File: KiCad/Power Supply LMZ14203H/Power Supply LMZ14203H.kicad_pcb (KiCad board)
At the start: 2 copper layers, 61 x 47 mm, 39 parts, among them J1 Power IN, J2 Conn_02x03_Odd_Even, J3 Power OUT, U1 INA169, U2 LMZ14203H, U3 MCP3428, U4 INA169

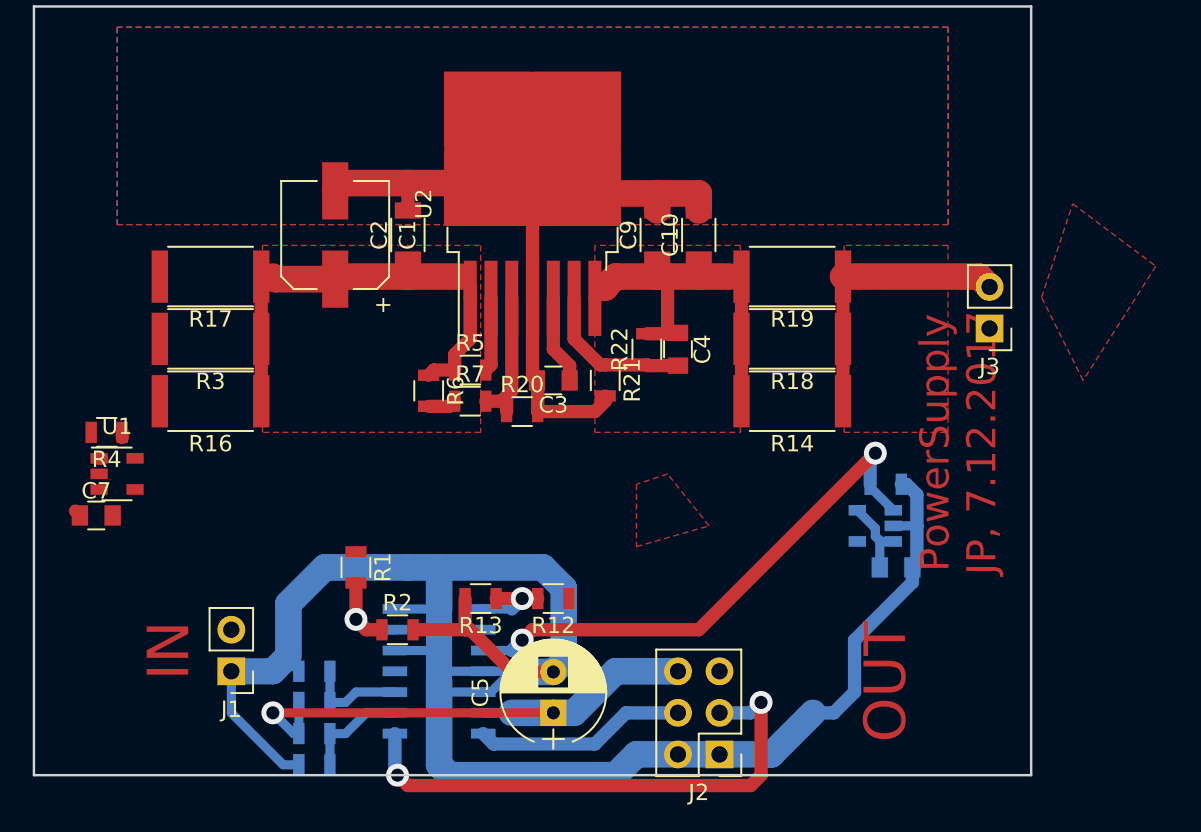
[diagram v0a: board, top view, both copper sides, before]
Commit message: LMZ14203H added
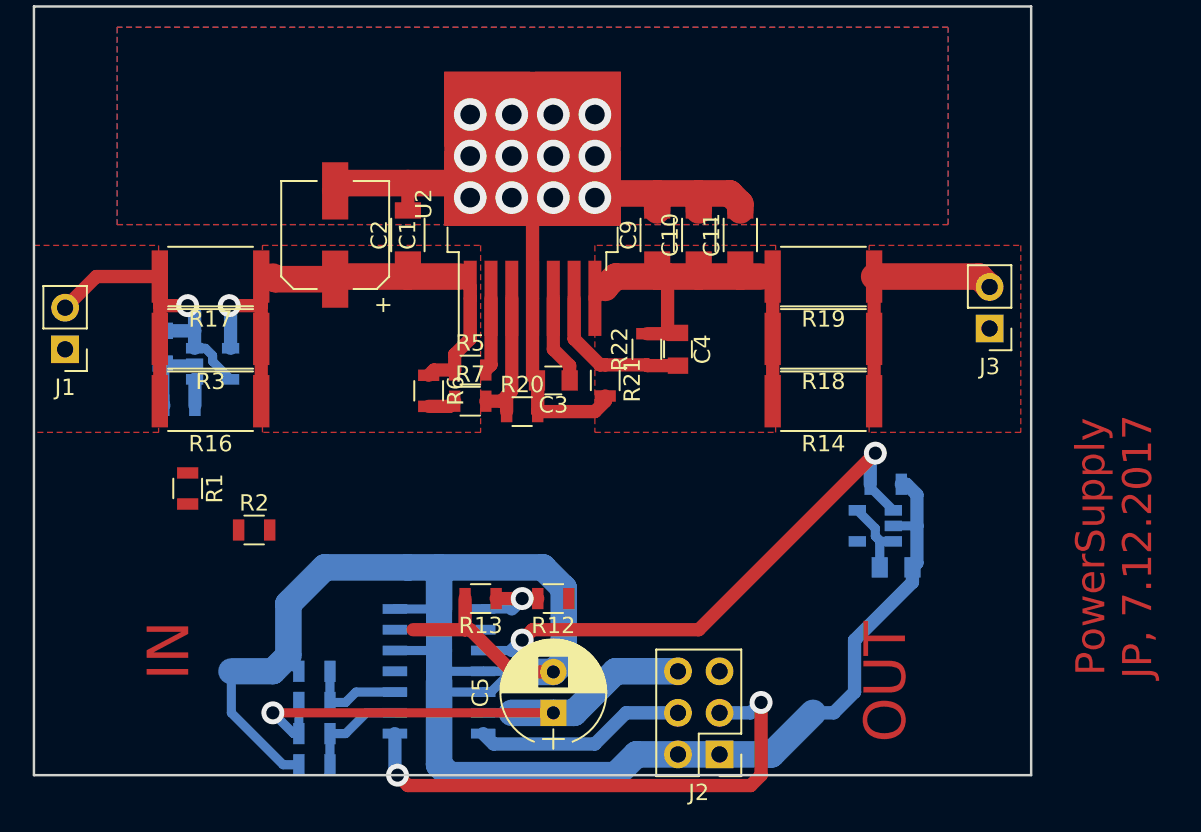
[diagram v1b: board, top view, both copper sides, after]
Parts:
- added C11: 47u/1-45mESR, Capacitors_SMD:C_1206, F.Cu at (161.3, 26.7)
- C7, R4, U1: moved to B.Cu
- moved J1 22.2 mm to (120.0, 33.7)
- moved R1 11.4 mm to (127.5, 42.2)
- moved C7 11.1 mm to (126.0, 33.5), turned to 90 degrees
- moved R2 10.7 mm to (131.6, 44.7)
- moved U1 8.91 mm to (129.0, 34.5)
- moved R4 4.74 mm to (127.0, 37.1)
- moved R14 1.91 mm to (166.4, 36.8)
- moved R18 1.91 mm to (166.4, 33.0)
- moved R19 1.91 mm to (166.4, 29.2)
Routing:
- net GNDA: track 181.8 -> 217.1 mm, vias 0 -> 12
- net Net-(C7-Pad2): track 0.00 -> 23.8 mm, vias 0 -> 1
- net IN_Voltage: track 6.72 -> 0.00 mm, vias 1 -> 0
- net Net-(C1-Pad1): track 29.0 -> 33.6 mm, vias 0 -> 1
- net Net-(C10-Pad1): track 31.2 -> 34.2 mm
- net Net-(J3-Pad2): track 16.8 -> 14.9 mm
- net IN_Current: track 0.46 -> 1.60 mm
- added copper zone on F.Cu, net Net-(C7-Pad2)
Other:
- net class Default: via_drill 0.8 -> 0.6

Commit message: Wirering
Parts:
- removed J2: Conn_02x03_Odd_Even, Pin_Headers:Pin_Header_Straight_2x03_Pitch2.54mm
- added C12: 10n, Capacitors_SMD:C_0805, F.Cu at (155.3, 90.1)
- added C13: 100n, Capacitors_SMD:C_0805, B.Cu at (121.9, 49.5)
- added C14: 100u, Capacitors_SMD:CP_Elec_6.3x7.7, F.Cu at (123.8, 44.3)
- added C16: 100n, Capacitors_SMD:C_0805, B.Cu at (121.9, 58.4)
- added C17: 47u, Capacitors_SMD:CP_Elec_6.3x5.8, F.Cu at (119.2, 54.0)
- added C18: 100n, Capacitors_SMD:C_0805, B.Cu at (144.8, 54.6)
- added C19: 10u, Capacitors_SMD:CP_Elec_4x5.8, F.Cu at (144.8, 57.8)
- added C20: 100n, Capacitors_SMD:C_0805, B.Cu at (134.6, 44.5)
- added C21: 10u, Capacitors_SMD:CP_Elec_4x5.8, F.Cu at (134.0, 43.8)
- added C22: 10u, Capacitors_SMD:CP_Elec_4x5.8, F.Cu at (173.4, 57.1)
- added C23: 10u, Capacitors_SMD:CP_Elec_4x5.8, F.Cu at (168.3, 52.1)
- added C24: 1u, Capacitors_SMD:C_0805, F.Cu at (149.0, 61.6)
- added D1: LED, Diodes_SMD:D_0805, F.Cu at (139.7, 85.7)
- added J4: OLED I2C, Pin_Headers:Pin_Header_Straight_1x04_Pitch2.54mm, F.Cu at (132.7, 52.7)
- added J5: PDI, Pin_Headers:Pin_Header_Straight_2x03_Pitch2.54mm, F.Cu at (179.1, 42.5)
- added J6: OLED, JPConnectors:FPC_30, F.Cu at (158.8, 57.1)
- added L1: 10u, Inductors_SMD:L_0805, F.Cu at (131.4, 49.5)
- added R23: 10k, Resistors_SMD:R_0805, F.Cu at (170.1, 80.3)
- added R24: 10k, Resistors_SMD:R_0805, F.Cu at (158.7, 90.2)
- added R25: 1M, Resistors_SMD:R_0805, F.Cu at (163.3, 89.9)
- added R26: 0, Resistors_SMD:R_0805, F.Cu at (149.2, 41.3)
- added SW1: SW_DIP_x01, Buttons_Switches_SMD:SW_SPST_B3SL-1002P, F.Cu at (184.2, 71.1)
- added U5: UA78M33, TO_SOT_Packages_SMD:TO-252-2_Rectifier, B.Cu at (120.0, 54.0)
- added U6: ATXMEGA32E5-AU, Housings_QFP:TQFP-32_7x7mm_Pitch0.8mm, B.Cu at (141.6, 48.3)
- C5: value 10u -> 100u; footprint Capacitors_THT:CP_Radial_D6.3mm_P2.50mm -> Capacitors_SMD:CP_Elec_6.3x7.7
- J1, J3: footprint Pin_Headers:Pin_Header_Straight_1x02_Pitch2.54mm -> Connectors_Terminal_Blocks:TerminalBlock_Altech_AK300-2_P5.00mm
- R10, R9: value 0 -> 2k2
- R11, R8: value 0 -> 10k
- U3: value MCP3428 -> L78M12; footprint Housings_SOIC:SOIC-14_3.9x8.7mm_Pitch1.27mm -> TO_SOT_Packages_SMD:TO-252-2_Rectifier
- moved C5 34.9 mm to (116.8, 44.5), turned to 270 degrees
- moved C6 30.1 mm to (121.3, 40.6), turned to 180 degrees
- moved U3 24.3 mm to (120.0, 45.1)
- moved R9 19.4 mm to (119.4, 64.5)
- moved R13 16.6 mm to (159.4, 40.0)
- moved R12 16.0 mm to (163.2, 40.0)
- moved R8 15.8 mm to (122.4, 64.5)
- moved C8 14.8 mm to (163.2, 34.3), turned to 90 degrees
- moved R10 13.1 mm to (122.9, 61.5)
- moved U4 10.0 mm to (166.4, 34.9), turned to 0 degrees
- moved J1 9.92 mm to (118.4, 23.9), turned to 270 degrees
- moved R11 9.83 mm to (126.5, 63.5)
- moved R2 7.70 mm to (138.1, 40.6)
- moved R15 7.24 mm to (164.5, 37.5), turned to 180 degrees
- moved R1 4.04 mm to (131.4, 41.3)
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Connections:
- C5 pad 1: +5V -> POWER_IN
- C5 pad 2: GNDA -> GND
- C6 pad 1: +5V -> POWER_IN
- C6 pad 2: GNDA -> GND
- C7 pad 2: Net-(C7-Pad2) -> POWER_IN
- J1 pad 2: Net-(C7-Pad2) -> POWER_IN
- J3 pad 1: GNDA -> POWER_OUT
- J3 pad 2: Net-(J3-Pad2) -> GNDA
- R1 pad 1: Net-(C7-Pad2) -> POWER_IN
- R10 pad 1: +5V -> SDA
- R10 pad 2: Net-(R10-Pad2) -> +3V3
- R11 pad 1: Net-(R10-Pad2) -> SWITCH
- R11 pad 2: GNDA -> Net-(R11-Pad2)
- R14 pad 1: Net-(J3-Pad2) -> POWER_OUT
- R16 pad 2: Net-(C7-Pad2) -> POWER_IN
- R17 pad 2: Net-(C7-Pad2) -> POWER_IN
- R18 pad 1: Net-(J3-Pad2) -> POWER_OUT
- R19 pad 1: Net-(J3-Pad2) -> POWER_OUT
- R3 pad 2: Net-(C7-Pad2) -> POWER_IN
- R8 pad 1: +5V -> LED
- R8 pad 2: Net-(R8-Pad2) -> Net-(D1-Pad1)
- R9 pad 1: Net-(R8-Pad2) -> SCK
- R9 pad 2: GNDA -> +3V3
- U1 pad 3: Net-(C7-Pad2) -> POWER_IN
- U1 pad 5: Net-(C7-Pad2) -> POWER_IN
- U3 pad 1: OUT_Voltage -> POWER_IN
- U3 pad 2: GNDA -> GND
- U3 pad 3: OUT_Current -> +12V
- U4 pad 4: Net-(J3-Pad2) -> POWER_OUT
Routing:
- net GNDA: track 217.1 -> 128.9 mm
- net GND: track 0.00 -> 54.0 mm, vias 0 -> 1
- net POWER_IN: track 0.00 -> 42.2 mm, vias 0 -> 1
- net /OLED_D4: track 0.00 -> 38.0 mm, vias 0 -> 1
- net /OLED_D2: track 0.00 -> 37.1 mm, vias 0 -> 1
- net /OLED_D0: track 0.00 -> 36.2 mm, vias 0 -> 3
- net +5V: track 36.1 -> 0.00 mm, vias 1 -> 0
- net /OLED_D6: track 0.00 -> 35.0 mm, vias 0 -> 1
- net SCL: track 32.6 -> 0.00 mm, vias 2 -> 0
- net OUT_Current: track 33.2 -> 1.65 mm, vias 2 -> 0
- net /OLED_D1: track 0.00 -> 31.4 mm, vias 0 -> 1
- net /OLED_D7: track 0.00 -> 30.5 mm, vias 0 -> 1
- net /OLED_D5: track 0.00 -> 26.1 mm, vias 0 -> 1
- net Net-(C7-Pad2): track 23.8 -> 0.00 mm, vias 1 -> 0
- net /OLED_D3: track 0.00 -> 22.9 mm, vias 0 -> 1
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- added copper zone on F.Cu, net POWER_IN
- added copper zone on F.Cu, net POWER_OUT
- removed copper zone on F.Cu, net Net-(C7-Pad2)
- removed copper zone on F.Cu, net Net-(J3-Pad2)
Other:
- board size 61 x 47 mm -> 71.8 x 51.4 mm
- board text removed: "IN"

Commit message: Wirering done
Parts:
- added REF**: MountingHole_3.2mm_M3, Mounting_Holes:MountingHole_3.2mm_M3, F.Cu at (122.6, 54.0)
- added REF**: MountingHole_3.2mm_M3, Mounting_Holes:MountingHole_3.2mm_M3, F.Cu at (59.7, 54.0)
- added REF**: MountingHole_3.2mm_M3, Mounting_Holes:MountingHole_3.2mm_M3, F.Cu at (61.0, 105.4)
- added REF**: MountingHole_3.2mm_M3, Mounting_Holes:MountingHole_3.2mm_M3, F.Cu at (122.6, 106.0)
- C24, L1, R1, R12, R13, R2, R24, R25: moved to B.Cu
- J4: footprint Pin_Headers:Pin_Header_Straight_1x04_Pitch2.54mm -> JPDisplays:OLED_0.96inch_128x64_I2C
- R11, R8: moved to F.Cu
- moved R12 87.1 mm to (88.3, 84.5), turned to 270 degrees
- moved R13 85.5 mm to (86.4, 84.5), turned to 90 degrees
- moved J5 78.9 mm to (118.1, 92.7), turned to 90 degrees
- moved J4 72.9 mm to (65.4, 80.6)
- moved C13 72.3 mm to (65.4, 94.6)
- moved C14 72.3 mm to (67.3, 89.4)
- moved C16 72.3 mm to (65.4, 103.5)
- moved C17 72.3 mm to (62.7, 99.1)
- moved C5 72.3 mm to (60.3, 89.5)
- moved C6 72.3 mm to (64.8, 85.7)
- moved J6 72.3 mm to (102.2, 102.2)
- moved U3 72.3 mm to (63.5, 90.2)
- moved U5 72.3 mm to (63.5, 99.1)
- moved U6 72.3 mm to (85.1, 93.3)
- moved C21 72.1 mm to (79.0, 90.5), turned to 0 degrees
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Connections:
- net Net-(C20-Pad1) renamed /+3.3VA
- C7 pad 1: GNDA -> GND
- C8 pad 1: GNDA -> GND
- J5 pad 3: (no net) -> Net-(J5-Pad3)
- J5 pad 4: (no net) -> Net-(J5-Pad4)
- J6 pad 18: (no net) -> Net-(J6-Pad18)
- J6 pad 22: (no net) -> Net-(J6-Pad22)
- J6 pad 23: (no net) -> Net-(J6-Pad23)
- J6 pad 24: (no net) -> Net-(J6-Pad24)
- J6 pad 25: (no net) -> Net-(J6-Pad25)
- J6 pad 26: (no net) -> Net-(J6-Pad26)
- J6 pad 27: (no net) -> Net-(J6-Pad27)
- J6 pad 28: (no net) -> Net-(J6-Pad28)
- J6 pad 30: (no net) -> Net-(J6-Pad30)
- R13 pad 2: GNDA -> GND
- R15 pad 2: GNDA -> GND
- R2 pad 2: GNDA -> GND
- R4 pad 2: GNDA -> GND
- U1 pad 2: GNDA -> GND
- U4 pad 2: GNDA -> GND
- U6 pad 19: (no net) -> Net-(U6-Pad19)
- U6 pad 2: (no net) -> Net-(U6-Pad2)
- U6 pad 20: (no net) -> Net-(U6-Pad20)
- U6 pad 26: (no net) -> Net-(U6-Pad26)
- U6 pad 3: OUT_Current -> IN_Current
- U6 pad 31: (no net) -> Net-(U6-Pad31)
- U6 pad 4: OUT_Voltage -> IN_Voltage
- U6 pad 5: IN_Current -> OUT_Voltage
- U6 pad 6: IN_Voltage -> OUT_Current
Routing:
- net GND: track 54.0 -> 247.9 mm, vias 1 -> 9
- net +3V3: track 8.83 -> 123.5 mm, vias 1 -> 6
- net +12V: track 18.7 -> 70.4 mm, vias 1 -> 2
- net PDI_DATA: track 0.00 -> 45.1 mm, vias 0 -> 1
- net SWITCH: track 0.00 -> 39.5 mm, vias 0 -> 1
- net OUT_Current: track 1.65 -> 34.7 mm
- net Net-(C10-Pad1): track 38.8 -> 71.5 mm
- net PDI_CLK: track 0.00 -> 32.2 mm
- net /OLED_E/!RD: track 0.00 -> 30.4 mm, vias 0 -> 1
- net POWER_IN: track 42.2 -> 72.2 mm, vias 1 -> 2
- net /OLED_R/!W: track 0.00 -> 29.3 mm, vias 0 -> 1
- net /OLED_D/!C: track 0.00 -> 26.9 mm, vias 0 -> 1
- net /OLED_!RES: track 0.00 -> 25.8 mm, vias 0 -> 1
- net IN_Current: track 1.60 -> 23.9 mm
- net /OLED_!DS: track 0.00 -> 22.2 mm, vias 0 -> 1
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- added copper zone on B.Cu, net GND
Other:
- board size 71.8 x 51.4 mm -> 71.8 x 61 mm
- board text added: "In(35V)"
- board text added: "JP"
- board text added: "Out"
- board text added: "PowerSupplyLMZ v1 JP, 15.08.2018"
- board text removed: "OUT"
- board text removed: "PowerSupply JP, 7.12.2017"

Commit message: PCB proofing
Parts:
- removed C11: 47u/1-45mESR, Capacitors_SMD:C_1206
- added C15: 100n, Capacitors_SMD:C_0805, B.Cu at (88.3, 84.5)
- added C25: 100n, Capacitors_SMD:C_0805, B.Cu at (81.3, 85.1)
- added C26: 100n, Capacitors_SMD:C_0805, B.Cu at (90.8, 84.5)
- added C27: 100n, Capacitors_SMD:C_0805, F.Cu at (89.5, 88.9)
- added F1: 5A, Fuse_Holders_and_Fuses:Fuseholder5x20_horiz_open_inline_Type-I, F.Cu at (56.5, 74.9)
- added R27: 220k, Resistors_SMD:R_0805, F.Cu at (85.1, 71.8)
- added R28: 15k4, Resistors_SMD:R_0805, F.Cu at (101.0, 73.0)
- C10, C9: footprint Capacitors_SMD:C_1206 -> Capacitors_Tantalum_SMD:CP_Tantalum_Case-D_EIA-7343-31_Reflow
- C2: footprint Capacitors_SMD:C_1206 -> Capacitors_SMD:C_2220
- R21: value 2k43 -> 2k2
- R22: value 34k -> 15k4
- R25: footprint Resistors_SMD:R_0805 -> Resistors_SMD:R_1206
- R5: value 250k -> 30k
- SW1: footprint Buttons_Switches_SMD:SW_SPST_B3SL-1002P -> Buttons_Switches_SMD:SW_SPST_B3S-1000
- moved R12 6.35 mm to (94.6, 84.5)
- moved R13 6.35 mm to (92.7, 84.5)
- moved C8 5.08 mm to (111.8, 71.1)
- moved J3 5.08 mm to (125.7, 66.0)
- moved R14 5.08 mm to (114.9, 73.7)
- moved R15 5.08 mm to (113.0, 74.3)
- moved R18 5.08 mm to (114.9, 69.8)
- moved R19 5.08 mm to (114.9, 66.0)
- moved REF** 5.08 mm to (127.6, 54.0)
- moved SW1 5.08 mm to (125.7, 81.3)
- moved U4 5.08 mm to (114.9, 71.8)
- moved C10 4.45 mm to (106.7, 63.5)
- moved C12 4.45 mm to (118.7, 79.4)
- moved C17 4.45 mm to (67.2, 99.1)
- moved C18 4.45 mm to (94.0, 100.3)
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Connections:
- J1 pad 2: POWER_IN -> Net-(F1-Pad1)
- J5 pad 3: Net-(J5-Pad3) -> (no net)
- J5 pad 4: Net-(J5-Pad4) -> (no net)
- J6 pad 18: Net-(J6-Pad18) -> (no net)
- J6 pad 22: Net-(J6-Pad22) -> (no net)
- J6 pad 23: Net-(J6-Pad23) -> (no net)
- J6 pad 24: Net-(J6-Pad24) -> (no net)
- J6 pad 25: Net-(J6-Pad25) -> (no net)
- J6 pad 26: Net-(J6-Pad26) -> (no net)
- J6 pad 27: Net-(J6-Pad27) -> (no net)
- J6 pad 28: Net-(J6-Pad28) -> (no net)
- J6 pad 30: Net-(J6-Pad30) -> (no net)
- R22 pad 2: Net-(C10-Pad1) -> Net-(R22-Pad2)
- R5 pad 1: Net-(C1-Pad1) -> Net-(R27-Pad2)
- U6 pad 19: Net-(U6-Pad19) -> (no net)
- U6 pad 2: Net-(U6-Pad2) -> (no net)
- U6 pad 20: Net-(U6-Pad20) -> (no net)
- U6 pad 26: Net-(U6-Pad26) -> (no net)
- U6 pad 31: Net-(U6-Pad31) -> (no net)
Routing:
- net POWER_IN: track 72.2 -> 91.1 mm
- net Net-(F1-Pad1): track 0.00 -> 15.3 mm
- net GND: track 247.9 -> 258.7 mm
- net GNDA: track 122.0 -> 132.6 mm
- net IN_Current: track 23.9 -> 34.2 mm
- net OUT_Current: track 34.7 -> 42.6 mm, vias 0 -> 1
- net /OLED_D2: track 43.6 -> 36.3 mm
- net Net-(R11-Pad2): track 10.2 -> 12.2 mm
- net IN_Voltage: track 5.96 -> 7.86 mm
- net OUT_Voltage: track 5.96 -> 7.86 mm
- net Net-(R22-Pad2): track 0.00 -> 1.72 mm
- net Net-(C1-Pad1): track 33.6 -> 32.2 mm
- net Net-(R27-Pad2): track 0.00 -> 1.27 mm
- net /+3.3VA: track 10.6 -> 9.44 mm
- net /OLED_D3: track 22.7 -> 23.8 mm
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- added copper zone on B.Cu, net Net-(F1-Pad1)
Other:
- board size 71.8 x 61 mm -> 80 x 61.6 mm
- board text added: "PowerSupplyLMZ v1 JP, 20.08.2018"
- board text removed: "PowerSupplyLMZ v1 JP, 15.08.2018"

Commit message: PCB proofing
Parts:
- removed the REF** at (57.1, 105.4)
- removed the REF** at (127.0, 106.0)
- added REF**: RET012864LYPP3N, JPDisplays:RET012864LYPP3N, F.Cu at (91.4, 94.0)
- moved J5 15.5 mm to (135.3, 101.6), turned to 180 degrees
- moved R24 15.3 mm to (130.2, 102.9)
- moved C12 10.8 mm to (127.0, 86.4)
- moved R11 10.8 mm to (127.0, 88.3)
- moved R23 10.8 mm to (127.0, 90.2)
- moved SW1 9.16 mm to (133.3, 86.4), turned to 270 degrees
- moved J1 7.24 mm to (50.8, 61.0)
- moved REF** 7.10 mm to (50.2, 52.7)
- moved J3 6.35 mm to (132.1, 66.0)
- moved F1 5.43 mm to (58.4, 80.0)
- moved REF** 5.24 mm to (132.7, 52.7)
- moved C13 5.12 mm to (72.4, 99.1)
- moved C15 5.12 mm to (90.8, 88.9)
- moved C16 5.12 mm to (72.4, 108.0)
- moved C5 5.12 mm to (67.3, 94.0)
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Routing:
- net GNDA: track 132.6 -> 150.7 mm
- net GND: track 258.7 -> 273.4 mm
- net PDI_CLK: track 32.2 -> 46.5 mm
- net +3V3: track 123.5 -> 135.5 mm, vias 6 -> 4
- net Net-(F1-Pad1): track 15.3 -> 24.3 mm
- net POWER_IN: track 91.1 -> 99.9 mm
- net POWER_OUT: track 21.7 -> 28.0 mm
- net SWITCH: track 39.5 -> 44.3 mm, vias 1 -> 3
- net IN_Current: track 34.2 -> 38.8 mm
- net Net-(C10-Pad1): track 70.6 -> 66.2 mm
- net (no net): track 4.45 -> 1.91 mm
- net OUT_Current: track 42.6 -> 41.5 mm
- net Net-(R11-Pad2): track 12.2 -> 13.1 mm
- net PDI_DATA: track 45.1 -> 45.4 mm, vias 1 -> 0
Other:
- board size 80 x 61.6 mm -> 92.7 x 71.8 mm
- board text added: "PowerSupplyLMZ v1 JP, 21.08.2018"
- board text removed: "PowerSupplyLMZ v1 JP, 20.08.2018"

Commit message: PCB proofing
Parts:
- moved R25 2.54 mm to (117.5, 106.7)
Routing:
- net Net-(J6-Pad4): track 9.46 -> 7.18 mm
- net GND: track 273.4 -> 271.3 mm

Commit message: Some fixes
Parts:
- moved D1 5.08 mm to (85.7, 100.3), turned to 180 degrees
- moved C27 1.91 mm to (92.1, 91.4)
- moved C22 1.42 mm to (125.1, 108.0)
- moved C24 1.42 mm to (104.1, 109.2)
- moved J6 1.42 mm to (109.9, 108.0)
- moved R25 1.42 mm to (118.1, 108.0)
- moved C23 1.42 mm to (119.4, 101.6)
- moved C19 1.33 mm to (95.9, 104.8)
- moved R8 1.27 mm to (87.0, 97.8), turned to 270 degrees
- moved R26 0.64 mm to (96.5, 81.3)
- moved C21 0.48 mm to (85.7, 94.6)
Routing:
- net /OLED_D1: track 32.8 -> 26.0 mm
- net /OLED_D0: track 41.5 -> 36.0 mm
- net /OLED_D6: track 37.1 -> 41.2 mm
- net /OLED_D7: track 27.2 -> 31.0 mm
- net /OLED_!DS: track 22.2 -> 25.9 mm
- net /OLED_D2: track 36.3 -> 39.5 mm
- net +12V: track 70.4 -> 73.4 mm
- net /OLED_D4: track 41.2 -> 38.7 mm
- net /OLED_R/!W: track 29.3 -> 31.4 mm
- net /OLED_D5: track 23.7 -> 25.6 mm
- net SCK: track 21.7 -> 23.4 mm
- net /OLED_!RES: track 25.8 -> 27.1 mm
- net SDA: track 19.6 -> 20.8 mm
- net Net-(J6-Pad4): track 7.18 -> 8.18 mm
- net GNDA: track 150.7 -> 149.8 mm
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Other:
- net class Default: via_dia 1.4 -> 1.6; via_drill 0.6 -> 0.8
- net class Power: via_dia 2 -> 2.2
- board text added: "PowerSupplyLMZ v1 JP, 22.08.2018"
- board text removed: "PowerSupplyLMZ v1 JP, 21.08.2018"
